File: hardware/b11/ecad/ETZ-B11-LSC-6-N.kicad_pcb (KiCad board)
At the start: 2 copper layers, 131.5 x 85.8 mm, 44 parts, among them SW1 MX-Hotswap-1U, SW10 MX-Hotswap-1U, SW11 MX-Hotswap-1U, SW12 MX-Hotswap-1U, SW13 MX-Hotswap-1U, SW14 MX-Hotswap-1U, SW15 MX-Hotswap-1U, SW16 MX-Hotswap-1U, SW17 MX-Hotswap-1U, SW18 MX-Hotswap-1U, SW19 MX-Hotswap-1U, SW2 MX-Hotswap-1U, SW20 MX-Hotswap-1U, SW21 MX-Hotswap-1U, SW22 MX-Hotswap-1U, SW3 MX-Hotswap-1U, SW4 MX-Hotswap-1U, SW5 MX-Hotswap-1U, SW6 MX-Hotswap-1U, SW7 MX-Hotswap-1U, SW8 MX-Hotswap-1U, SW9 MX-Hotswap-1U

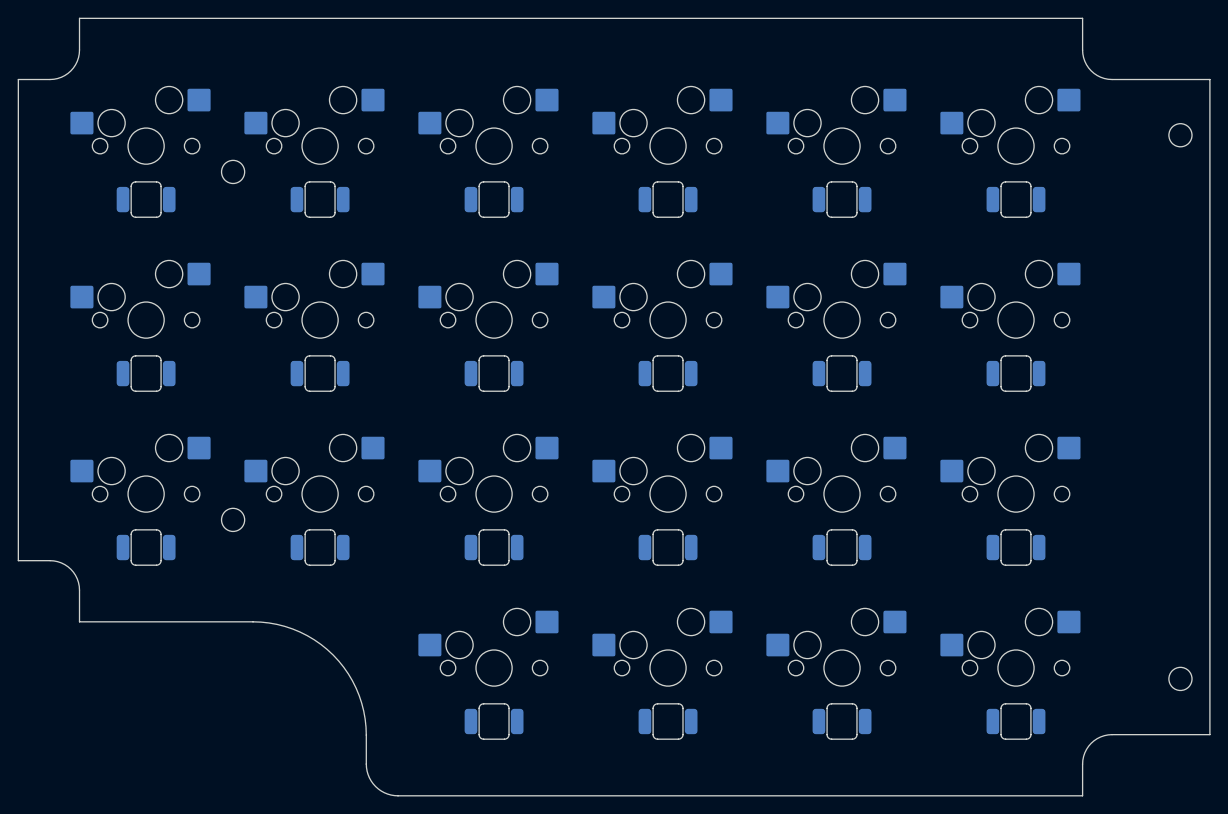
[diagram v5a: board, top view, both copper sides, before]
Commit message: fix(hardware/b11): adjust LED offset to 5.0mm and regenerate all carrier PCBs
Reduces south-facing LED offset from 5.9mm to 5.0mm (closer to the
standard 5.08mm switch-to-LED spacing). All 8 carrier PCBs regenerated.

Co-Authored-By: Claude Sonnet 4.6 <noreply@anthropic.com>
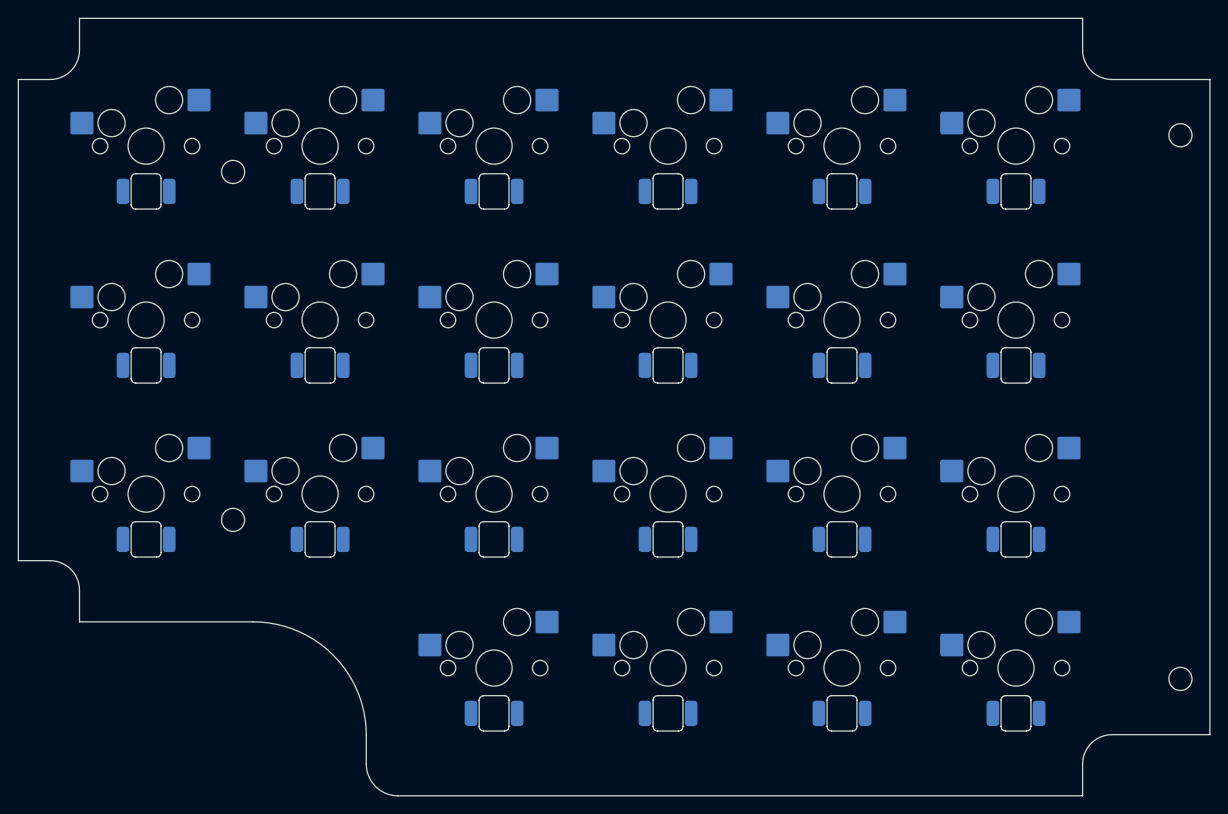
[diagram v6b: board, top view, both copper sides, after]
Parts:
- moved LED13 0.90 mm to (96.8, 116.7)
- moved LED14 0.90 mm to (116.0, 116.7)
- moved LED15 0.90 mm to (135.2, 116.7)
- moved LED16 0.90 mm to (154.4, 116.7)
- moved LED17 0.90 mm to (173.6, 116.7)
- moved LED18 0.90 mm to (192.8, 116.7)
- moved LED1 0.90 mm to (96.8, 78.3)
- moved LED10 0.90 mm to (154.4, 97.5)
- moved LED11 0.90 mm to (173.6, 97.5)
- moved LED12 0.90 mm to (192.8, 97.5)
- moved LED19 0.90 mm to (135.2, 135.9)
- moved LED2 0.90 mm to (116.0, 78.3)
- moved LED20 0.90 mm to (154.4, 135.9)
- moved LED21 0.90 mm to (173.6, 135.9)
- moved LED22 0.90 mm to (192.8, 135.9)
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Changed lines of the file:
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@@
 	(footprint "LED_SMD_6028_BackMount"
 		(layer "B.Cu")
-		(at 116.05 117.6)
+		(at 173.649999 116.699999)
 		(descr "SMD 6028 back-paste reverse-mount LED, 5.88x2.80mm body, 3.20mm lens, slot 3.3x6.2mm")
 		(tags "LED SMD 6028 reverse-mount back-paste backlighting Choc")
-		(property "Reference" "LED14"
+		(property "Reference" "LED17"
 			(at 0 -2 0)
 			(layer "B.Fab")
@@
 	(footprint "LED_SMD_6028_BackMount"
 		(layer "B.Cu")
-		(at 154.45 136.799999)
+		(at 173.649999 97.5)
 		(descr "SMD 6028 back-paste reverse-mount LED, 5.88x2.80mm body, 3.20mm lens, slot 3.3x6.2mm")
 		(tags "LED SMD 6028 reverse-mount back-paste backlighting Choc")
-		(property "Reference" "LED20"
+		(property "Reference" "LED11"
 			(at 0 -2 0)
 			(layer "B.Fab")
@@
 	(footprint "LED_SMD_6028_BackMount"
 		(layer "B.Cu")
-		(at 192.85 117.6)
+		(at 116.05 97.5)
 		(descr "SMD 6028 back-paste reverse-mount LED, 5.88x2.80mm body, 3.20mm lens, slot 3.3x6.2mm")
 		(tags "LED SMD 6028 reverse-mount back-paste backlighting Choc")
-		(property "Reference" "LED18"
+		(property "Reference" "LED8"
 			(at 0 -2 0)
 			(layer "B.Fab")
@@
 	(footprint "LED_SMD_6028_BackMount"
 		(layer "B.Cu")
-		(at 96.85 98.4)
+		(at 154.45 135.899999)
 		(descr "SMD 6028 back-paste reverse-mount LED, 5.88x2.80mm body, 3.20mm lens, slot 3.3x6.2mm")
 		(tags "LED SMD 6028 reverse-mount back-paste backlighting Choc")
-		(property "Reference" "LED7"
+		(property "Reference" "LED20"
 			(at 0 -2 0)
 			(layer "B.Fab")
@@
 	(footprint "LED_SMD_6028_BackMount"
 		(layer "B.Cu")
-		(at 135.25 117.6)
+		(at 135.25 135.899999)
 		(descr "SMD 6028 back-paste reverse-mount LED, 5.88x2.80mm body, 3.20mm lens, slot 3.3x6.2mm")
 		(tags "LED SMD 6028 reverse-mount back-paste backlighting Choc")
-		(property "Reference" "LED15"
+		(property "Reference" "LED19"
 			(at 0 -2 0)
 			(layer "B.Fab")
@@
 	(footprint "LED_SMD_6028_BackMount"
 		(layer "B.Cu")
-		(at 135.25 98.4)
+		(at 116.05 78.3)
 		(descr "SMD 6028 back-paste reverse-mount LED, 5.88x2.80mm body, 3.20mm lens, slot 3.3x6.2mm")
 		(tags "LED SMD 6028 reverse-mount back-paste backlighting Choc")
-		(property "Reference" "LED9"
+		(property "Reference" "LED2"
 			(at 0 -2 0)
 			(layer "B.Fab")
@@
 	(footprint "LED_SMD_6028_BackMount"
 		(layer "B.Cu")
-		(at 116.05 98.4)
+		(at 154.45 97.5)
 		(descr "SMD 6028 back-paste reverse-mount LED, 5.88x2.80mm body, 3.20mm lens, slot 3.3x6.2mm")
 		(tags "LED SMD 6028 reverse-mount back-paste backlighting Choc")
-		(property "Reference" "LED8"
+		(property "Reference" "LED10"
 			(at 0 -2 0)
 			(layer "B.Fab")
@@
 	(footprint "LED_SMD_6028_BackMount"
 		(layer "B.Cu")
-		(at 173.649999 117.6)
+		(at 96.85 78.3)
 		(descr "SMD 6028 back-paste reverse-mount LED, 5.88x2.80mm body, 3.20mm lens, slot 3.3x6.2mm")
 		(tags "LED SMD 6028 reverse-mount back-paste backlighting Choc")
-		(property "Reference" "LED17"
+		(property "Reference" "LED1"
 			(at 0 -2 0)
 			(layer "B.Fab")
@@
 	(footprint "LED_SMD_6028_BackMount"
 		(layer "B.Cu")
-		(at 173.649999 136.799999)
+		(at 135.25 78.3)
 		(descr "SMD 6028 back-paste reverse-mount LED, 5.88x2.80mm body, 3.20mm lens, slot 3.3x6.2mm")
 		(tags "LED SMD 6028 reverse-mount back-paste backlighting Choc")
-		(property "Reference" "LED21"
+		(property "Reference" "LED3"
 			(at 0 -2 0)
 			(layer "B.Fab")
@@
 	(footprint "LED_SMD_6028_BackMount"
 		(layer "B.Cu")
-		(at 96.85 117.6)
+		(at 154.45 116.699999)
 		(descr "SMD 6028 back-paste reverse-mount LED, 5.88x2.80mm body, 3.20mm lens, slot 3.3x6.2mm")
 		(tags "LED SMD 6028 reverse-mount back-paste backlighting Choc")
-		(property "Reference" "LED13"
+		(property "Reference" "LED16"
 			(at 0 -2 0)
 			(layer "B.Fab")
@@
 	(footprint "LED_SMD_6028_BackMount"
 		(layer "B.Cu")
-		(at 173.649999 79.2)
+		(at 135.25 97.5)
 		(descr "SMD 6028 back-paste reverse-mount LED, 5.88x2.80mm body, 3.20mm lens, slot 3.3x6.2mm")
 		(tags "LED SMD 6028 reverse-mount back-paste backlighting Choc")
-		(property "Reference" "LED5"
+		(property "Reference" "LED9"
 			(at 0 -2 0)
 			(layer "B.Fab")
@@
 	(footprint "LED_SMD_6028_BackMount"
 		(layer "B.Cu")
-		(at 192.85 79.2)
+		(at 192.85 78.3)
 		(descr "SMD 6028 back-paste reverse-mount LED, 5.88x2.80mm body, 3.20mm lens, slot 3.3x6.2mm")
 		(tags "LED SMD 6028 reverse-mount back-paste backlighting Choc")
@@
 	(footprint "LED_SMD_6028_BackMount"
 		(layer "B.Cu")
-		(at 135.25 136.799999)
+		(at 154.45 78.3)
 		(descr "SMD 6028 back-paste reverse-mount LED, 5.88x2.80mm body, 3.20mm lens, slot 3.3x6.2mm")
 		(tags "LED SMD 6028 reverse-mount back-paste backlighting Choc")
-		(property "Reference" "LED19"
+		(property "Reference" "LED4"
 			(at 0 -2 0)
 			(layer "B.Fab")
@@
 	(footprint "LED_SMD_6028_BackMount"
 		(layer "B.Cu")
-		(at 154.45 98.4)
+		(at 173.649999 135.899999)
 		(descr "SMD 6028 back-paste reverse-mount LED, 5.88x2.80mm body, 3.20mm lens, slot 3.3x6.2mm")
 		(tags "LED SMD 6028 reverse-mount back-paste backlighting Choc")
-		(property "Reference" "LED10"
+		(property "Reference" "LED21"
 			(at 0 -2 0)
 			(layer "B.Fab")
@@
 	(footprint "LED_SMD_6028_BackMount"
 		(layer "B.Cu")
-		(at 154.45 117.6)
+		(at 192.85 135.899999)
 		(descr "SMD 6028 back-paste reverse-mount LED, 5.88x2.80mm body, 3.20mm lens, slot 3.3x6.2mm")
 		(tags "LED SMD 6028 reverse-mount back-paste backlighting Choc")
-		(property "Reference" "LED16"
+		(property "Reference" "LED22"
 			(at 0 -2 0)
 			(layer "B.Fab")
@@
 	(footprint "LED_SMD_6028_BackMount"
 		(layer "B.Cu")
-		(at 154.45 79.2)
+		(at 173.649999 78.3)
 		(descr "SMD 6028 back-paste reverse-mount LED, 5.88x2.80mm body, 3.20mm lens, slot 3.3x6.2mm")
 		(tags "LED SMD 6028 reverse-mount back-paste backlighting Choc")
-		(property "Reference" "LED4"
+		(property "Reference" "LED5"
 			(at 0 -2 0)
 			(layer "B.Fab")
@@
 	(footprint "LED_SMD_6028_BackMount"
 		(layer "B.Cu")
-		(at 192.85 136.799999)
+		(at 135.25 116.699999)
 		(descr "SMD 6028 back-paste reverse-mount LED, 5.88x2.80mm body, 3.20mm lens, slot 3.3x6.2mm")
 		(tags "LED SMD 6028 reverse-mount back-paste backlighting Choc")
-		(property "Reference" "LED22"
+		(property "Reference" "LED15"
 			(at 0 -2 0)
 			(layer "B.Fab")
@@
 	(footprint "LED_SMD_6028_BackMount"
 		(layer "B.Cu")
-		(at 135.25 79.2)
+		(at 96.85 116.699999)
 		(descr "SMD 6028 back-paste reverse-mount LED, 5.88x2.80mm body, 3.20mm lens, slot 3.3x6.2mm")
 		(tags "LED SMD 6028 reverse-mount back-paste backlighting Choc")
-		(property "Reference" "LED3"
+		(property "Reference" "LED13"
 			(at 0 -2 0)
 			(layer "B.Fab")
@@
 	(footprint "LED_SMD_6028_BackMount"
 		(layer "B.Cu")
-		(at 116.05 79.2)
+		(at 192.85 97.5)
 		(descr "SMD 6028 back-paste reverse-mount LED, 5.88x2.80mm body, 3.20mm lens, slot 3.3x6.2mm")
 		(tags "LED SMD 6028 reverse-mount back-paste backlighting Choc")
-		(property "Reference" "LED2"
+		(property "Reference" "LED12"
 			(at 0 -2 0)
 			(layer "B.Fab")
@@
 	(footprint "LED_SMD_6028_BackMount"
 		(layer "B.Cu")
-		(at 192.85 98.4)
+		(at 96.85 97.5)
 		(descr "SMD 6028 back-paste reverse-mount LED, 5.88x2.80mm body, 3.20mm lens, slot 3.3x6.2mm")
 		(tags "LED SMD 6028 reverse-mount back-paste backlighting Choc")
-		(property "Reference" "LED12"
+		(property "Reference" "LED7"
 			(at 0 -2 0)
 			(layer "B.Fab")
@@
 	(footprint "LED_SMD_6028_BackMount"
 		(layer "B.Cu")
-		(at 173.649999 98.4)
+		(at 116.05 116.699999)
 		(descr "SMD 6028 back-paste reverse-mount LED, 5.88x2.80mm body, 3.20mm lens, slot 3.3x6.2mm")
 		(tags "LED SMD 6028 reverse-mount back-paste backlighting Choc")
-		(property "Reference" "LED11"
+		(property "Reference" "LED14"
 			(at 0 -2 0)
 			(layer "B.Fab")
@@
 	(footprint "LED_SMD_6028_BackMount"
 		(layer "B.Cu")
-		(at 96.85 79.2)
+		(at 192.85 116.699999)
 		(descr "SMD 6028 back-paste reverse-mount LED, 5.88x2.80mm body, 3.20mm lens, slot 3.3x6.2mm")
 		(tags "LED SMD 6028 reverse-mount back-paste backlighting Choc")
-		(property "Reference" "LED1"
+		(property "Reference" "LED18"
 			(at 0 -2 0)
 			(layer "B.Fab")
